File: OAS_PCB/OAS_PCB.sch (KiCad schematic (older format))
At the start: 3 parts

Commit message: test pushing change to PCB
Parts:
- AS?: symbol OAS_lib:AS3394 -> OAS_PCB-rescue:AS3394-OAS_lib
- DAC?: symbol OAS_lib:DAC8580IPW -> OAS_PCB-rescue:DAC8580IPW-OAS_lib
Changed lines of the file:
@@
 $EndComp
 $Comp
-L OAS_lib:DAC8580IPW DAC?
+L OAS_PCB-rescue:DAC8580IPW-OAS_lib DAC?
 U 1 1 5FC8E69F
 P 1550 1500
@@
 Text Label 2850 6600 0    50   ~ 0
 m7
-Text Label 3900 5450 2    50   ~ 0
+Text Label 5100 3000 2    50   ~ 0
 m0
-Text Label 3900 6050 2    50   ~ 0
+Text Label 5100 3600 2    50   ~ 0
 m1
-Text Label 3900 6200 2    50   ~ 0
+Text Label 5100 3750 2    50   ~ 0
 m2
+Text Label 5100 3900 2    50   ~ 0
+m3
+Text Label 6500 4500 0    50   ~ 0
+m4
+Text Label 6500 4200 0    50   ~ 0
+m5
+Text Label 6500 3450 0    50   ~ 0
+m6
+Text Label 6500 3150 0    50   ~ 0
+m7
 $Comp
-L OAS_lib:AS3394 AS?
+L OAS_PCB-rescue:AS3394-OAS_lib AS?
 U 1 1 5FC85A98
-P 4600 5950
-F 0 "AS?" H 4600 6825 50  0000 C CNN
-F 1 "AS3394" H 4600 6734 50  0000 C CNN
-F 2 "" H 4650 6150 50  0001 C CNN
-F 3 "" H 4650 6150 50  0001 C CNN
-	1    4600 5950
+P 5800 3500
+F 0 "AS?" H 5800 4375 50  0000 C CNN
+F 1 "AS3394" H 5800 4284 50  0000 C CNN
+F 2 "" H 5850 3700 50  0001 C CNN
+F 3 "" H 5850 3700 50  0001 C CNN
+	1    5800 3500
 	1    0    0    -1
 $EndComp
-Text Label 3900 6350 2    50   ~ 0
-m3
-Text Label 5300 6950 0    50   ~ 0
-m4
-Text Label 5300 6650 0    50   ~ 0
-m5
-Text Label 5300 5900 0    50   ~ 0
-m6
-Text Label 5300 5600 0    50   ~ 0
-m7
 $EndSCHEMATC

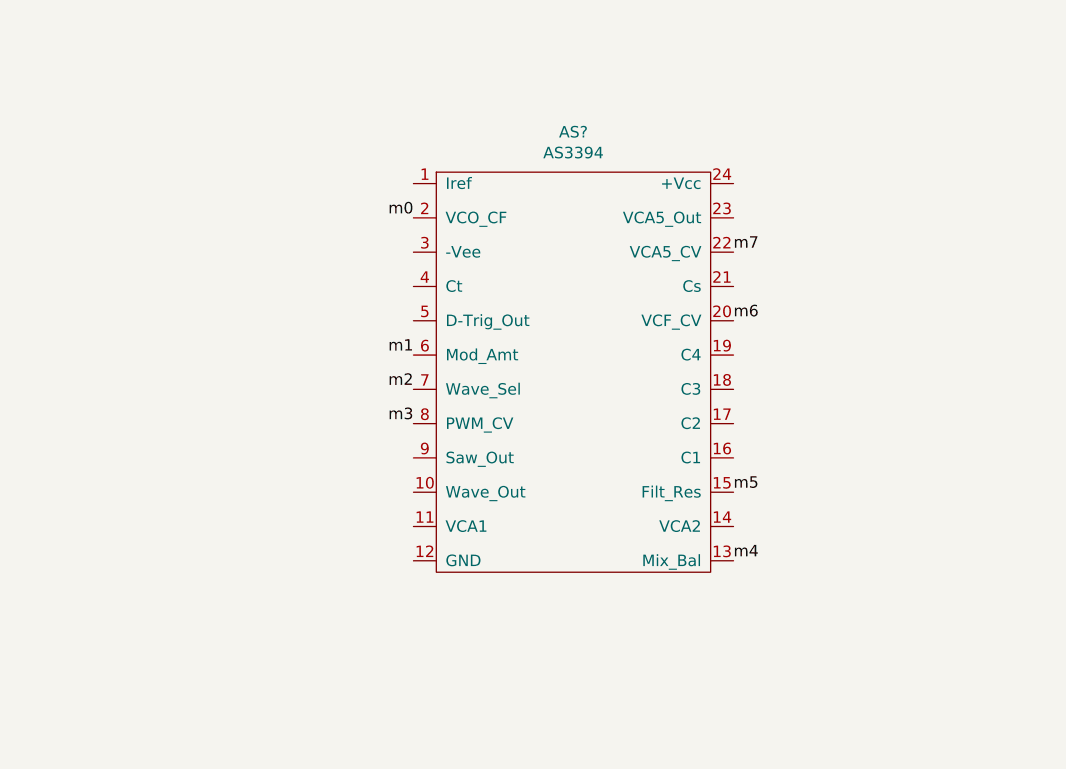
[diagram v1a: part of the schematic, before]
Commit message: Drafted the external components connecting to the AS3394 chip.
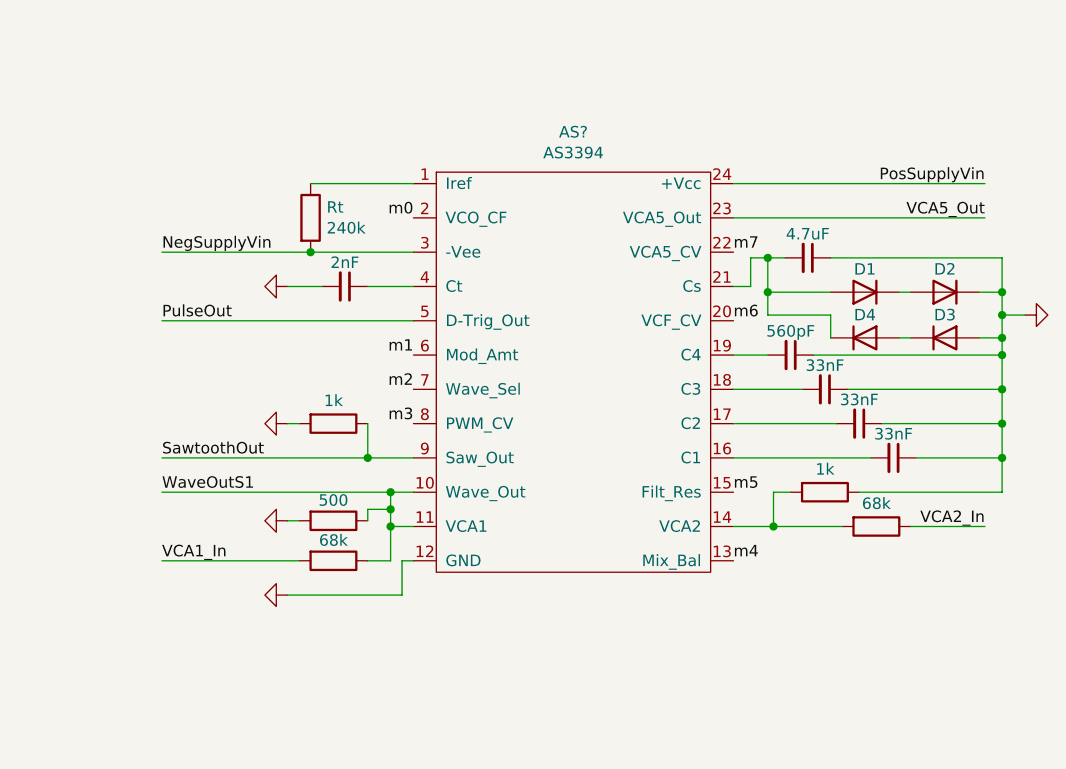
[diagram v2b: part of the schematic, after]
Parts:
- added C1, C2, C3: 33nF, symbol Device:C_Small
- added C4: 560pF, symbol Device:C_Small
- added Cs: 4.7uF, symbol Device:C_Small
- added Ct: 2nF, symbol Device:C_Small
- added D1, D2, D3, D4: DIODE, symbol Simulation_SPICE:DIODE
- added R (x2): 1k, symbol Device:R
- added R? (x2): 68k, symbol Device:R
- added R?: 500, symbol Device:R
- added Rt: 240k, symbol Device:R
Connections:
- net at AS?.1 (Iref): now also Rt.1
- net WaveOutS1: now reaches AS?.10 (Wave_Out)
- net WaveOutS1: now also AS?.11 (VCA1), R?.1, R?.1
- net GND: now reaches AS?.12 (GND)
- net GND: now also C1.1, C2.1, C3.1, C4.1, Cs.1, Ct.2, D2.2 (K), D3.1 (A), R.1, R.2, R?.2
- net at AS?.14 (VCA2): now also R.2, R?.2
- net at AS?.16 (C1): now also C1.2
- net at AS?.17 (C2): now also C2.2
- net at AS?.18 (C3): now also C3.2
- net at AS?.19 (C4): now also C4.2
- net at AS?.21 (Cs): now also Cs.2, D1.1 (A), D4.2 (K)
- net VCA5_Out: now reaches AS?.23 (VCA5_Out)
- net PosSupplyVin: now reaches AS?.24 (+Vcc)
- net NegSupplyVin: now reaches AS?.3 (-Vee)
- net NegSupplyVin: now also Rt.2
- net at AS?.4 (Ct): now also Ct.1
- net PulseOut: now reaches AS?.5 (D-Trig_Out)
- net SawtoothOut: now reaches AS?.9 (Saw_Out)
- net SawtoothOut: now also R.1
- new net: D1.2 (K), D2.1 (A)
- new net: D3.2 (K), D4.1 (A)
- new net VCA1_In: R?.2
- new net VCA2_In: R?.1
